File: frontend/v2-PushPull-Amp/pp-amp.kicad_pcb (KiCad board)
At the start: 4 copper layers, 80 x 100 mm, 165 parts, among them K1 HK4100, K10 HK4100, K11 HK4100, K12 HK4100, K13 HK4100, K14 HK4100, K15 HK4100, K2 HK4100, K3 HK4100, K4 HK4100, K5 HK4100, K6 HK4100, K7 HK4100, K8 HK4100, K9 HK4100, P1 Antenna, P2 CONN_02X07, P3 TX Power Tap, P4 TX-IN, P5 RX IN, P6 12-13.8v, Q1 PZT2222A, Q2 RD16HHF1, T1 OUT_TRANSF, T2 BN-43-2402, U1 LP2951-50D

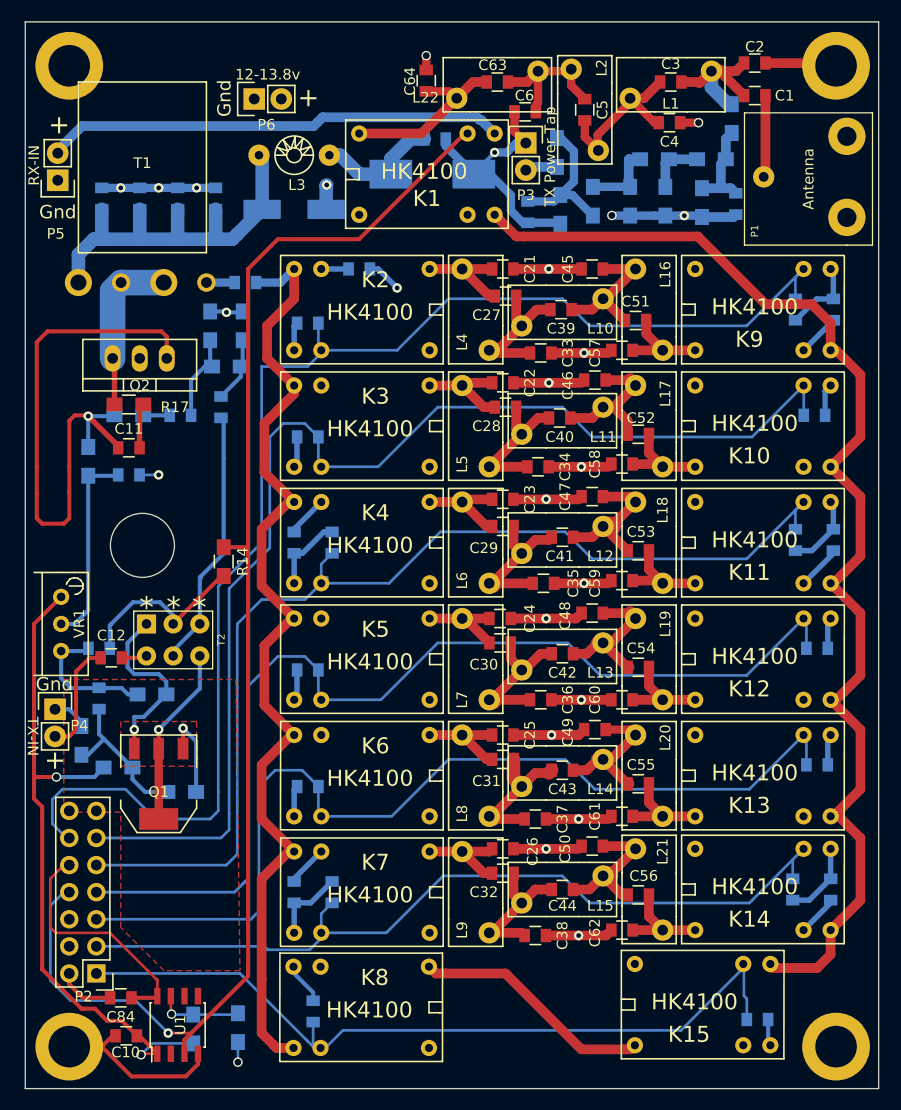
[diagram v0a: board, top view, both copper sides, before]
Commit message: Went back to using input transformer with 50R unbalanced input
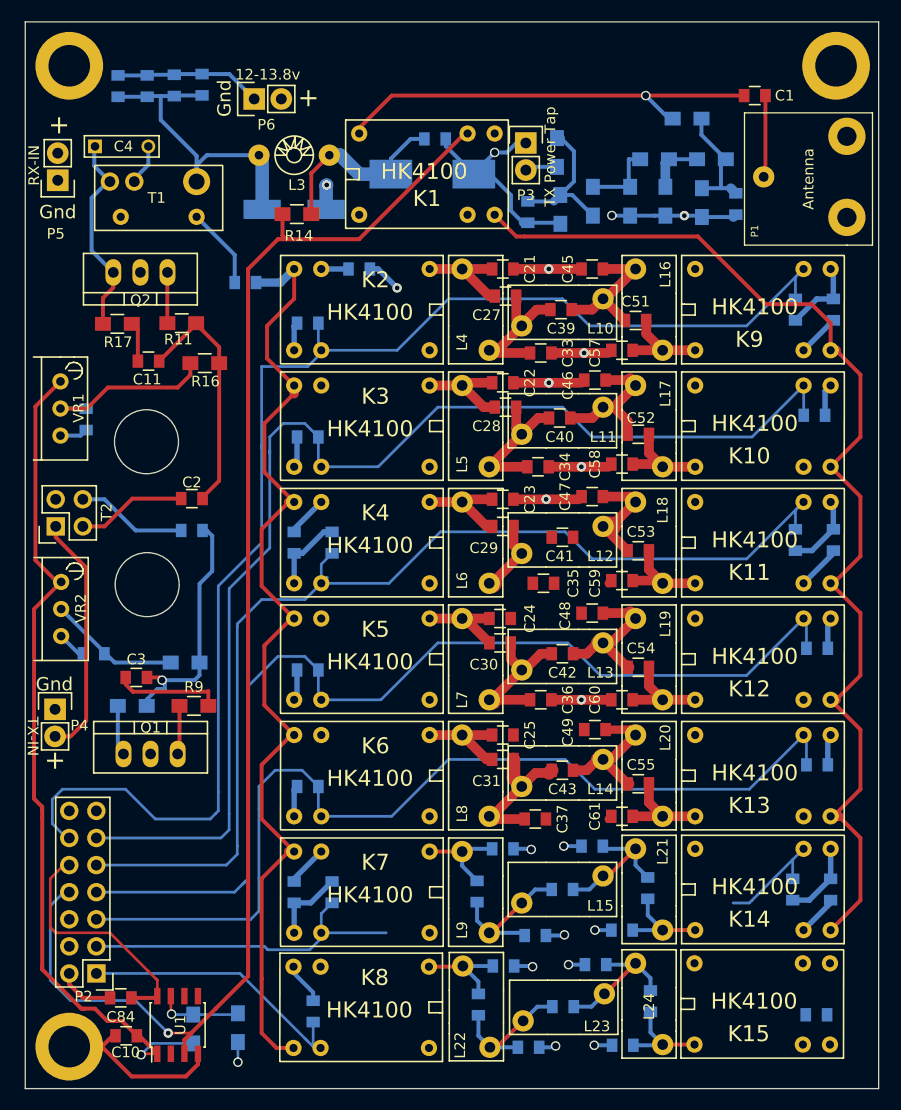
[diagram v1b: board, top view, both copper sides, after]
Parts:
- removed L1: 363nH, HERMESLITE:Choke_Toroid
- removed L2: 243nH, HERMESLITE:Choke_Toroid
- removed R12: 270, Resistors_SMD:R_0805_HandSoldering
- removed R13: 4.7, Resistors_SMD:R_0805_HandSoldering
- removed R15: 6.8, Resistors_SMD:R_0805_HandSoldering
- removed R18: 47, Resistors_SMD:R_0805_HandSoldering
- added L23: 243nH, HERMESLITE:Choke_Toroid, F.Cu at (160.4, 129.9)
- added L24: 363nH, HERMESLITE:Choke_Toroid, F.Cu at (170.9, 122.0)
- added MountingHole_6mm: VAL**, Mounting_Holes:MountingHole_6mm, F.Cu at (126.4, 87.8)
- added VR2: 1k MT, Potentiometers:Potentiometer_Bourns_3296W_3-8Zoll_Inline_ScrewUp, F.Cu at (118.4, 87.5)
- C12, C26, C32, C38, C44, C50, C56, C62: moved to B.Cu
- C2: value 82pf -> 0.1uF
- C3: value DNI -> 0.1uF
- C4: value 150pf -> 150pF; footprint HERMESLITE:C_0805 -> Capacitors_ThroughHole:C_Rect_L7_W2_P5
- C5: value 56pf -> 82pf; moved to B.Cu
- C6: value 150pf -> DNI; moved to B.Cu
- C63: value DNI -> 56pf; moved to B.Cu
- C64: value 82pF -> 150pf; moved to B.Cu
- C8: value 0.1uF -> 150pf
- C85: value 0.1uF -> DNI
- C86: value 0.1uF -> 82pF
- Q1: value PZT2222A -> RD16HHF1; footprint TO_SOT_Packages_SMD:SOT-223 -> TO_SOT_Packages_THT:TO-220_Neutral123_Vertical
- Q2: footprint Transistors_TO-220:TO-220_Neutral123_Vertical -> TO_SOT_Packages_THT:TO-220_Neutral123_Vertical
- R10: value 18 -> 2.2
- R11: value 1k -> 2.2; moved to F.Cu
- R16: moved to F.Cu
- R8: value 270 -> 10k
- R9: value 1.2k -> 270; moved to F.Cu
- T1: value OUT_TRANSF -> TRANSFO4; footprint HERMESLITE:OUT_TRANSF -> HERMESLITE:OUT_TRANSF_PP
- T2: value BN-43-2402 -> TRANSFO; footprint HERMESLITE:TRANSF -> Pin_Headers:Pin_Header_Straight_2x02
- moved C63 86.9 mm to (165.4, 127.3), turned to 180 degrees
- moved L22 84.4 mm to (154.7, 122.2), turned to 270 degrees
- moved C64 84.4 mm to (168.5, 123.4), turned to 180 degrees
- moved C6 83.8 mm to (157.5, 127.1), turned to 90 degrees
- moved C5 80.6 mm to (159.8, 123.5), turned to 0 degrees
- moved C3 75.0 mm to (125.4, 96.5)
- moved C86 70.7 mm to (171.0, 130.9), turned to 180 degrees
- moved C8 67.6 mm to (162.2, 131.1)
- moved C2 66.7 mm to (130.6, 79.7)
- moved C85 59.0 mm to (173.6, 126.8)
- moved C4 53.9 mm to (121.5, 46.7)
- moved R11 40.2 mm to (129.7, 63.2), turned to 0 degrees
- moved R14 33.3 mm to (140.5, 53.0), turned to 0 degrees
- moved R10 33.0 mm to (125.0, 99.1)
- moved R8 32.0 mm to (130.0, 95.1), turned to 180 degrees
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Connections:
- C2 pad 1: Net-(C1-Pad2) -> Net-(C2-Pad1)
- C2 pad 2: GND -> Net-(C11-Pad2)
- C3 pad 2: Net-(C1-Pad2) -> Net-(C12-Pad2)
- C4 pad 1: Net-(C3-Pad1) -> Net-(C4-Pad1)
- C4 pad 2: GND -> Net-(C4-Pad2)
- C5 pad 2: Net-(C3-Pad1) -> GND
- C6 pad 1: Net-(C5-Pad1) -> Net-(C6-Pad1)
- C6 pad 2: GND -> Net-(C5-Pad1)
- C63 pad 2: Net-(C5-Pad1) -> Net-(C6-Pad1)
- C8 pad 1: Net-(C8-Pad1) -> Net-(C6-Pad1)
- C8 pad 2: Net-(C8-Pad2) -> GND
- C85 pad 2: GND -> Net-(C63-Pad1)
- C86 pad 1: Net-(C86-Pad1) -> Net-(C85-Pad1)
- C86 pad 2: Net-(C86-Pad2) -> GND
- C87 pad 2: +12v -> Net-(C87-Pad2)
- K1 pad 3: Net-(C63-Pad1) -> Net-(C1-Pad2)
- K15 pad 4: Net-(K15-Pad4) -> Net-(C85-Pad1)
- K8 pad 4: Net-(K15-Pad4) -> Net-(C5-Pad1)
- L22 pad 2: Net-(C63-Pad1) -> Net-(C6-Pad1)
- P4 pad 2: Net-(C12-Pad1) -> Net-(P4-Pad2)
- Q1 pad 2: Net-(Q1-Pad2) -> GND
- Q1 pad 3: Net-(Q1-Pad3) -> Net-(C4-Pad2)
- Q2 pad 1: Net-(C11-Pad2) -> Net-(Q2-Pad1)
- Q2 pad 3: Net-(Q2-Pad3) -> Net-(C4-Pad1)
- R10 pad 1: Net-(C8-Pad2) -> Net-(Q1-Pad1)
- R10 pad 2: Net-(C86-Pad2) -> Net-(C12-Pad2)
- R11 pad 1: GND -> Net-(Q2-Pad1)
- R11 pad 2: Net-(C85-Pad1) -> Net-(C11-Pad2)
- R17 pad 1: Net-(Q2-Pad3) -> Net-(C4-Pad1)
- R8 pad 1: GND -> Net-(C12-Pad2)
- R8 pad 2: Net-(C86-Pad2) -> Net-(C87-Pad2)
- R9 pad 1: Net-(C85-Pad1) -> Net-(C4-Pad2)
- R9 pad 2: Net-(C10-Pad2) -> Net-(C3-Pad1)
- T1 pad 1: Net-(C16-Pad2) -> Net-(C4-Pad2)
- T1 pad 2: Net-(Q2-Pad3) -> Net-(C16-Pad2)
- T1 pad 3: Net-(Q2-Pad3) -> Net-(C4-Pad1)
- T1 pad 4: Net-(C15-Pad1) -> GND
- T2 pad 1: Net-(Q1-Pad3) -> Net-(P4-Pad2)
- T2 pad 2: Net-(C12-Pad2) -> GND
- T2 pad 3: +12v -> Net-(C2-Pad1)
- T2 pad 4: Net-(C86-Pad1) -> Net-(C12-Pad1)
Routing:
- net GND: track 266.6 -> 194.8 mm, vias 25 -> 20
- net /Band6: track 76.1 -> 28.2 mm
- net Net-(K1-Pad1): track 43.5 -> 0.61 mm
- net /Band5: track 77.8 -> 42.0 mm
- net Net-(C11-Pad2): track 55.5 -> 23.0 mm, vias 1 -> 0
- net +12v: track 380.7 -> 355.7 mm
- net Net-(C1-Pad2): track 16.3 -> 41.3 mm, vias 0 -> 1
- net Net-(C86-Pad1): track 24.5 -> 0.00 mm
- net Net-(P4-Pad2): track 0.00 -> 23.8 mm
- net Net-(K15-Pad4): track 22.7 -> 0.00 mm
- net Net-(C12-Pad2): track 2.62 -> 23.5 mm, vias 0 -> 1
- net Net-(C4-Pad1): track 0.00 -> 19.3 mm
- net Net-(Q1-Pad3): track 17.1 -> 0.00 mm, vias 1 -> 0
- net Net-(Q1-Pad2): track 16.9 -> 0.00 mm, vias 1 -> 0
- net Net-(Q2-Pad3): track 15.8 -> 0.00 mm
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- removed copper zone on F.Cu, net Net-(Q1-Pad2)
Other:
- board text removed: "*"
